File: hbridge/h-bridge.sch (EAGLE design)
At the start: 7 parts

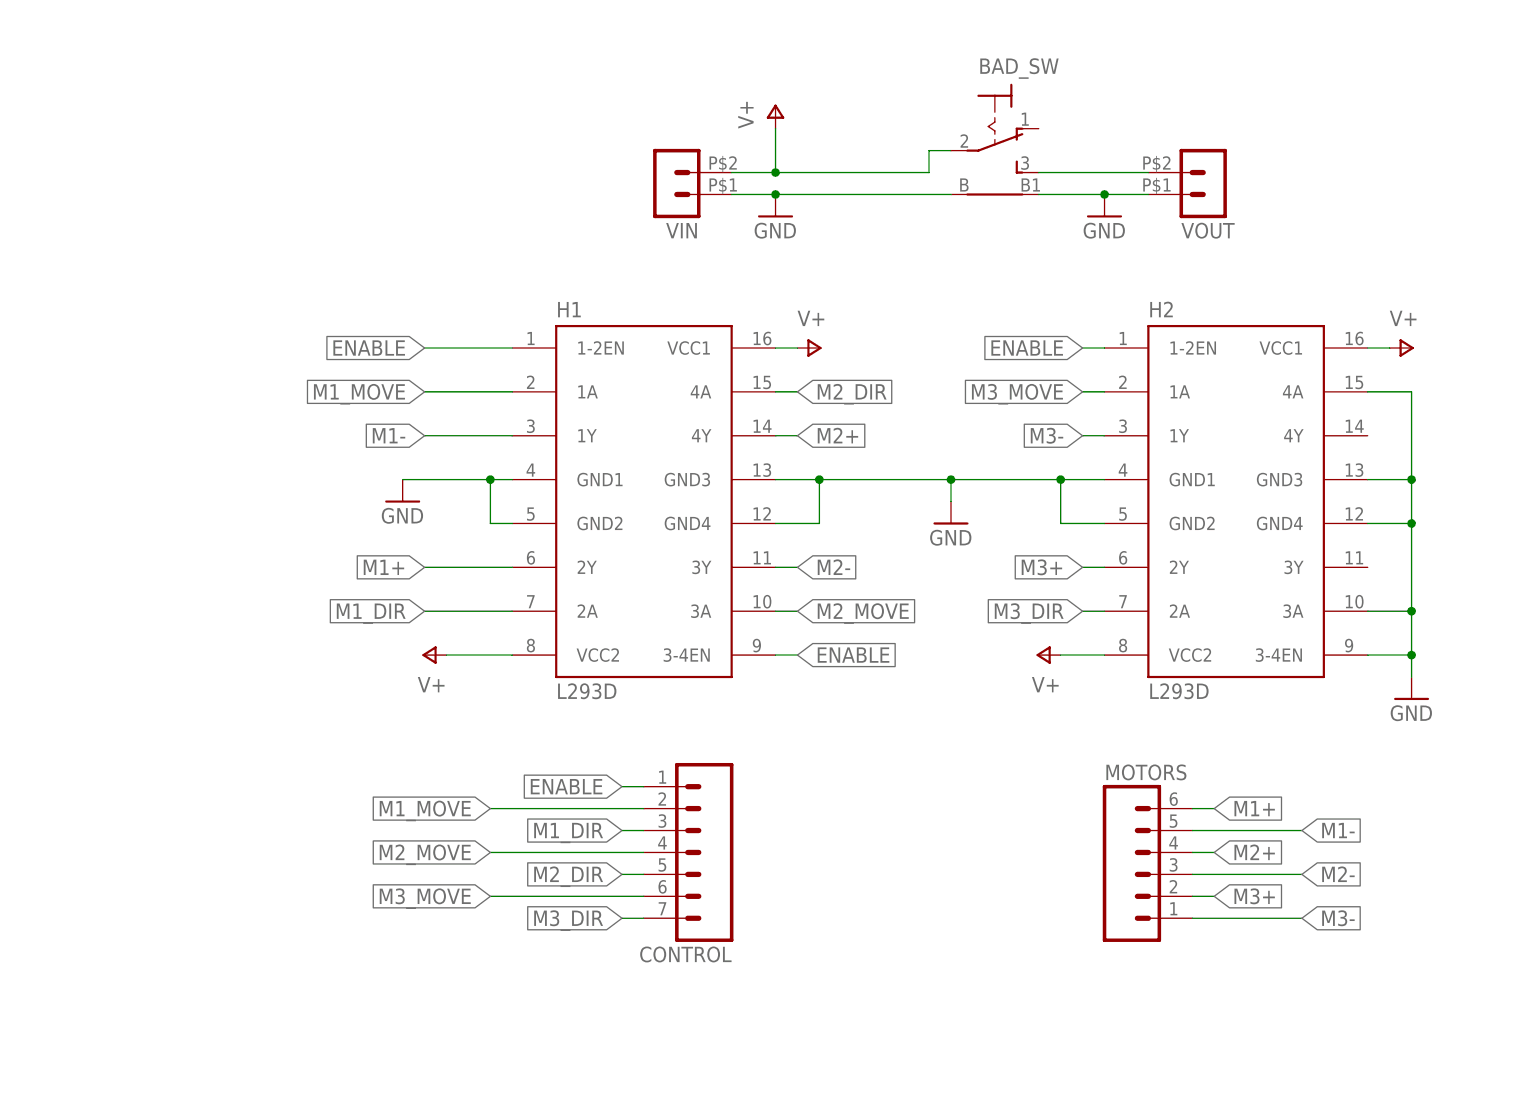
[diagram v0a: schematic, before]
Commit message: Rework H-bridge to add charge port, move headers to back
- correct hole sizes and placement
- added key dimension documentation
- switch toggles battery between circuit and charge port
- headers on backside leading toward center of chassis
- battery in and daisy chain output also point into center
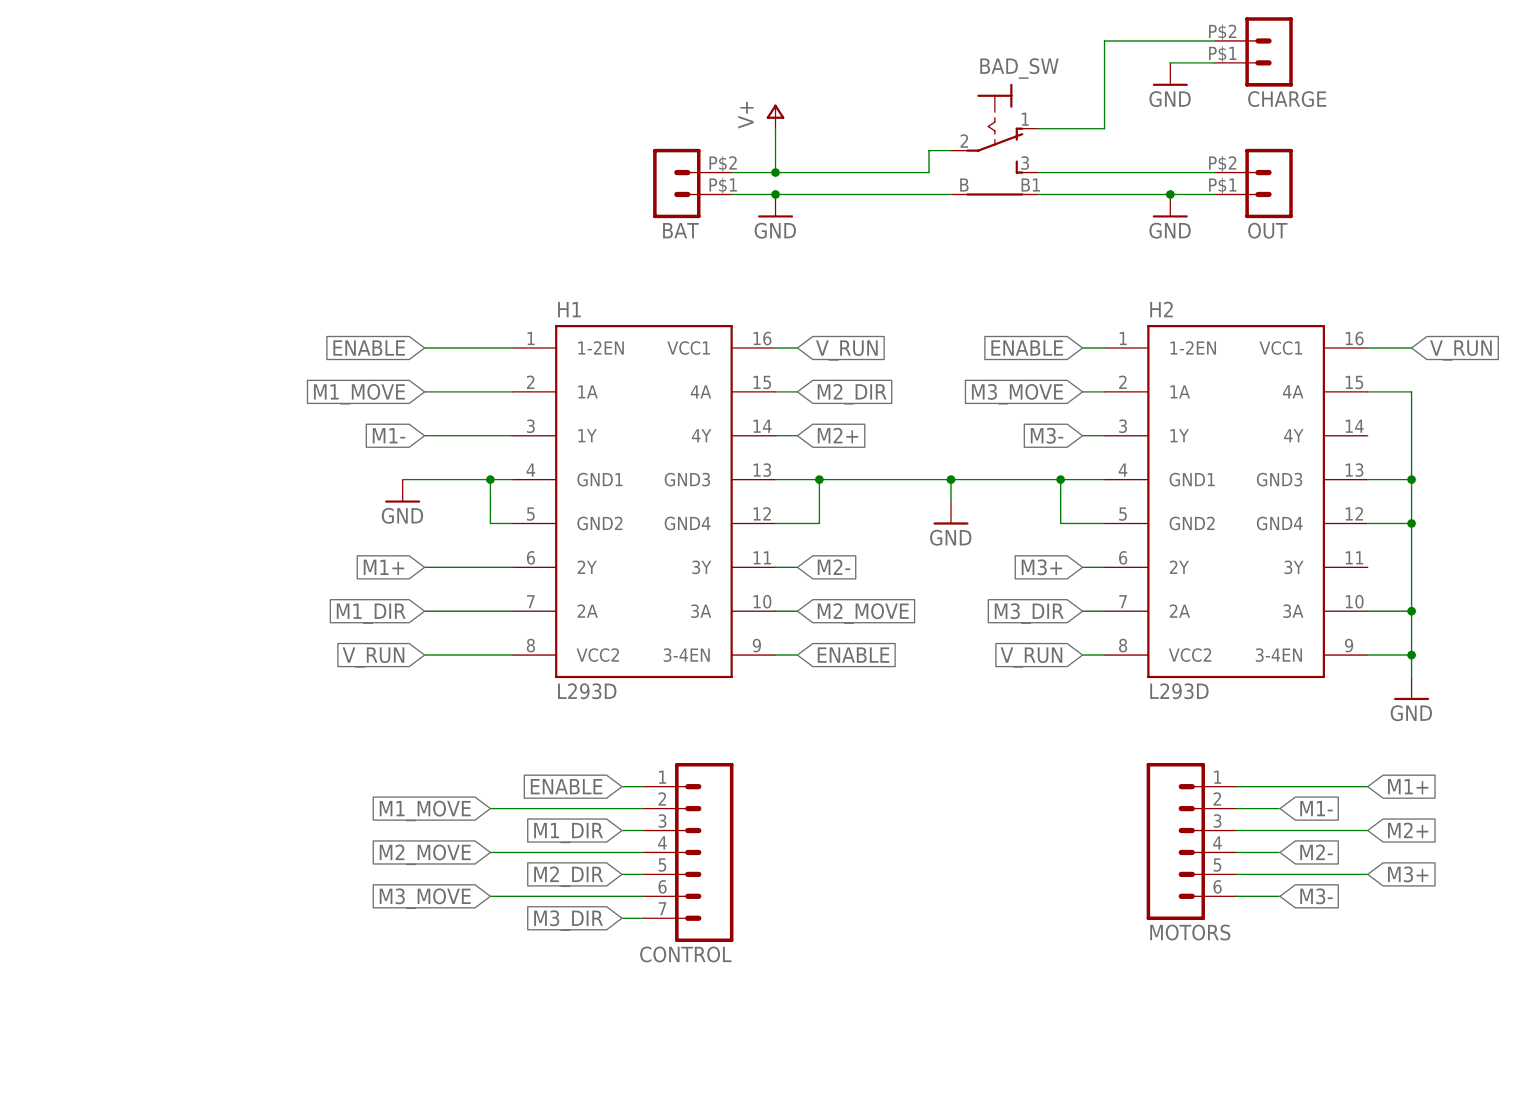
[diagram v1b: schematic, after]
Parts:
- removed VOUT: (no value), con-molex-micro-fit-3_0:HEADER_POS2_43045-0206
- added CHARGE, OUT: (no value), con-molex-micro-fit-3_0:HEADER_POS2_43045-0206
- CONTROL: device SparkFun-Connectors:M07LOCK_LONGPADS -> SparkFun-Connectors:M07LOCK
- MOTORS: device SparkFun-Connectors:M06LOCK_LONGPADS -> SparkFun-Connectors:M06LOCK
- renumbered VIN to BAT
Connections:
- removed net N$3: BAD_SW.S, VOUT.2
- new net V_CHARGE: BAD_SW.O, CHARGE.2
- new net V_RUN: BAD_SW.S, H1.VCC1, OUT.2
- net GND: now also CHARGE.1, OUT.1; no longer VOUT.1
- net M1+: now also MOTORS.1; no longer MOTORS.6
- net M1-: now also MOTORS.2; no longer MOTORS.5
- net M2+: now also MOTORS.3; no longer MOTORS.4
- net M2-: now also MOTORS.4; no longer MOTORS.3
- net M3+: now also MOTORS.5; no longer MOTORS.2
- net M3-: now also MOTORS.6; no longer MOTORS.1
- net V+: no longer H1.VCC1, H1.VCC2, H2.VCC1, H2.VCC2
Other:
- moved on the sheet: MOTORS

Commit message: Fix V_RUN net so that it is actually attached to ICs
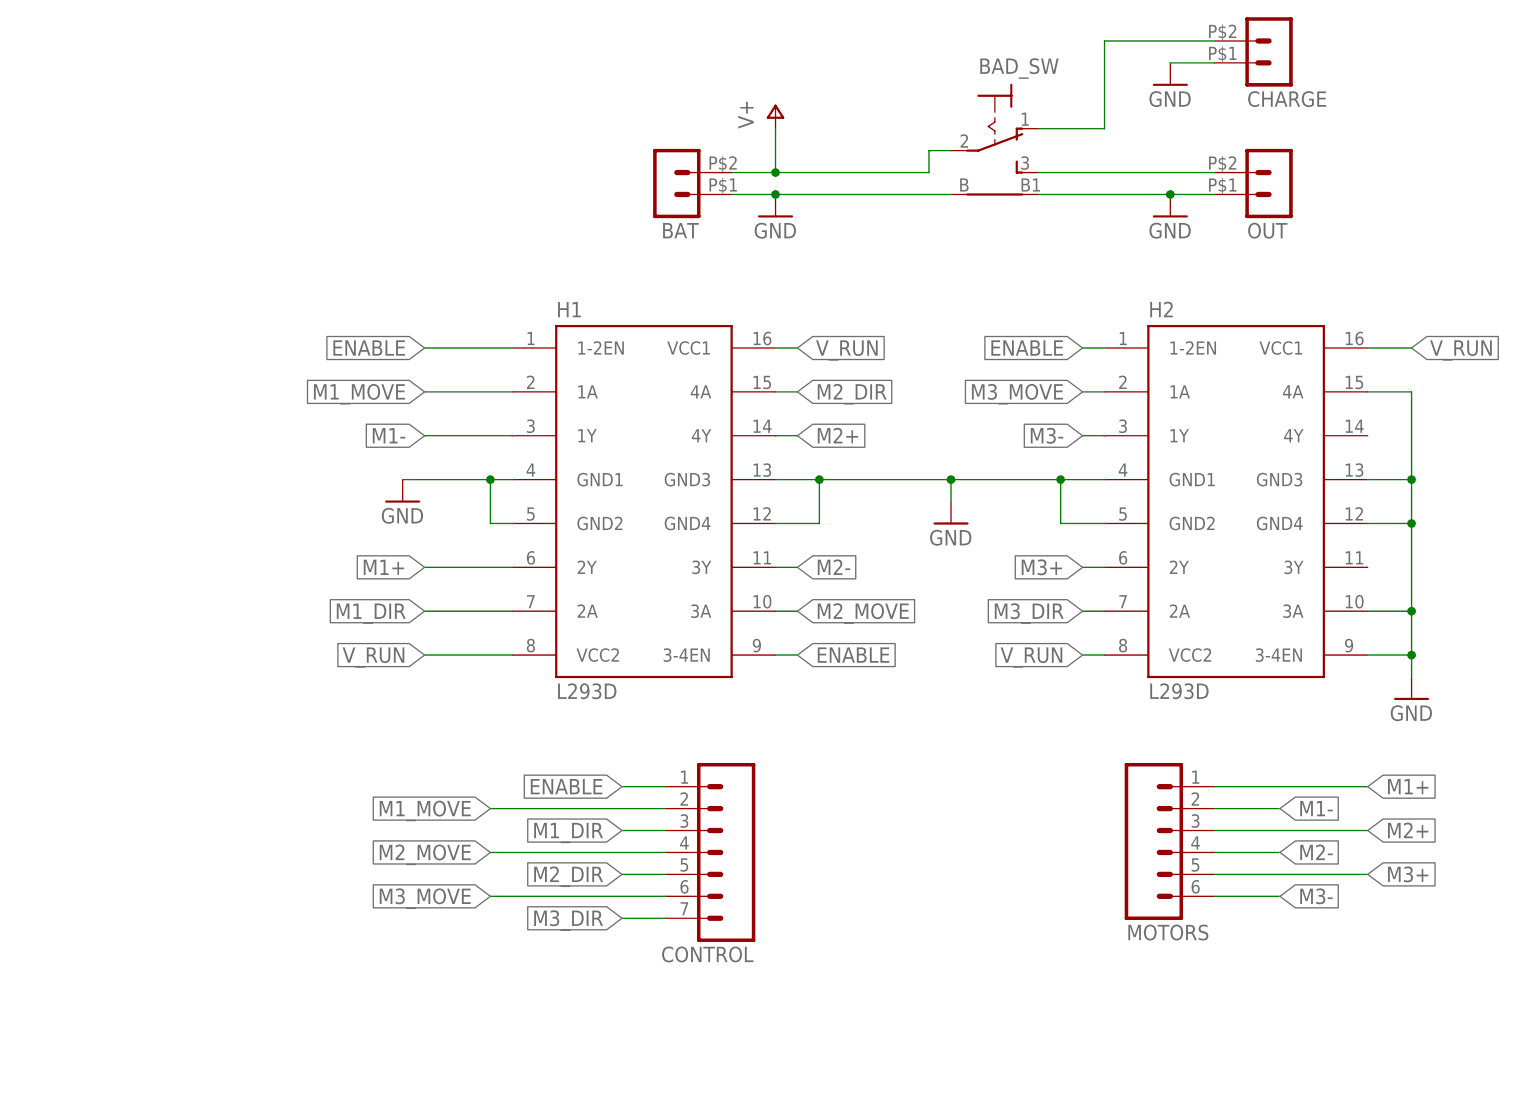
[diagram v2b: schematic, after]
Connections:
- net V_RUN: now also H1.VCC2, H2.VCC1, H2.VCC2
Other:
- moved on the sheet: CONTROL, MOTORS

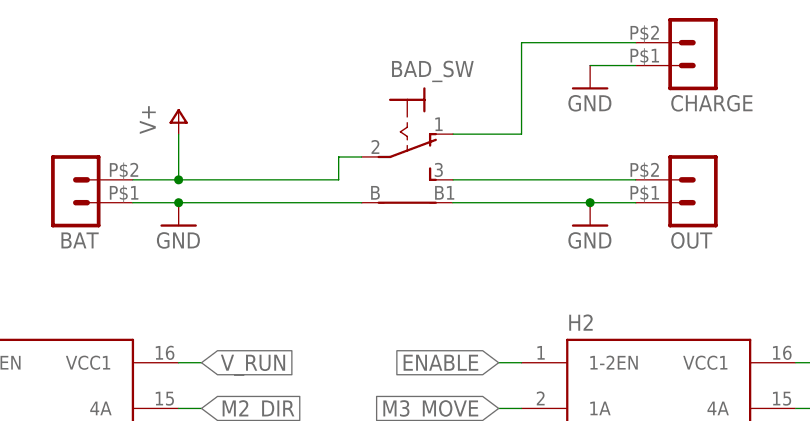
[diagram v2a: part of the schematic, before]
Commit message: Update H-bridge board to use correct switch
- The E-switch WSP1 is a custom model from the wolfbot.lbr library
- Shifted most components due to the larger switch footprint
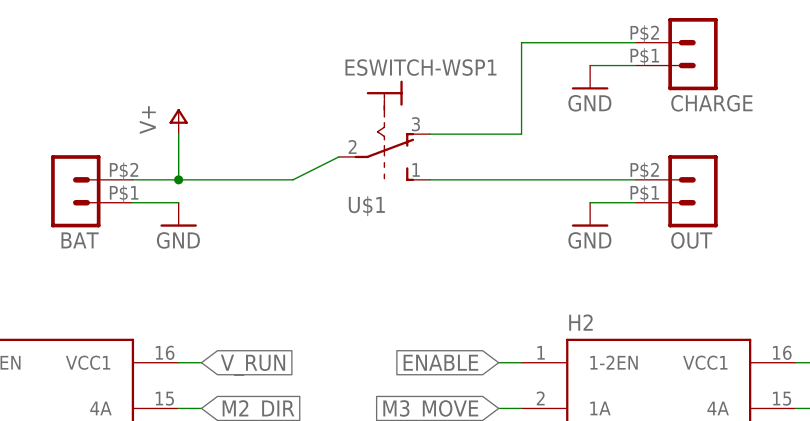
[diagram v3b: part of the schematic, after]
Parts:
- removed BAD_SW: (no value), switch:9070-1W
- added U$1: ESWITCH-WSP1, wolfbot:ESWITCH-WSP1
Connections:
- net GND: no longer BAD_SW.B, BAD_SW.B1
- net V+: now also U$1.2; no longer BAD_SW.P
- net V_CHARGE: now also U$1.3; no longer BAD_SW.O
- net V_RUN: now also U$1.1; no longer BAD_SW.S
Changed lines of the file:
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@@
 <part name="GND4" library="supply1" deviceset="GND" device=""/>
 <part name="GND5" library="supply1" deviceset="GND" device=""/>
-<part name="BAD_SW" library="switch" deviceset="9070-1W" device=""/>
 <part name="GND3" library="supply1" deviceset="GND" device=""/>
 <part name="CHARGE" library="con-molex-micro-fit-3_0" deviceset="HEADER_POS2_?" device="43045-0206"/>
 <part name="GND6" library="supply1" deviceset="GND" device=""/>
+<part name="U$1" library="wolfbot" deviceset="ESWITCH-WSP1" device=""/>
 </parts>
 <sheets>
@@
 <instance part="GND4" gate="1" x="20.32" y="71.12"/>
 <instance part="GND5" gate="1" x="137.16" y="48.26"/>
-<instance part="BAD_SW" gate="2" x="88.9" y="114.3" rot="R270"/>
 <instance part="GND3" gate="1" x="109.22" y="104.14"/>
 <instance part="CHARGE" gate="G$1" x="119.38" y="124.46" rot="MR180"/>
 <instance part="GND6" gate="1" x="109.22" y="119.38"/>
+<instance part="U$1" gate="G$1" x="83.82" y="111.76"/>
 </instances>
 <busses>
@@
 <pinref part="GND2" gate="1" pin="GND"/>
 <wire x1="58.42" y1="106.68" x2="63.5" y2="106.68" width="0.1524" layer="91"/>
-<pinref part="BAD_SW" gate="2" pin="B"/>
-<wire x1="63.5" y1="106.68" x2="83.82" y2="106.68" width="0.1524" layer="91"/>
-<junction x="63.5" y="106.68"/>
-</segment>
-<segment>
-<pinref part="BAD_SW" gate="2" pin="B1"/>
+</segment>
+<segment>
 <pinref part="OUT" gate="G$1" pin="1"/>
-<wire x1="93.98" y1="106.68" x2="109.22" y2="106.68" width="0.1524" layer="91"/>
 <pinref part="GND3" gate="1" pin="GND"/>
 <wire x1="109.22" y1="106.68" x2="114.3" y2="106.68" width="0.1524" layer="91"/>
-<junction x="109.22" y="106.68"/>
 </segment>
 <segment>
@@
 <pinref part="P+1" gate="1" pin="V+"/>
 <wire x1="63.5" y1="114.3" x2="63.5" y2="109.22" width="0.1524" layer="91"/>
-<wire x1="63.5" y1="109.22" x2="81.28" y2="109.22" width="0.1524" layer="91"/>
+<wire x1="63.5" y1="109.22" x2="76.2" y2="109.22" width="0.1524" layer="91"/>
 <junction x="63.5" y="109.22"/>
-<pinref part="BAD_SW" gate="2" pin="P"/>
-<wire x1="83.82" y1="111.76" x2="81.28" y2="111.76" width="0.1524" layer="91"/>
-<wire x1="81.28" y1="111.76" x2="81.28" y2="109.22" width="0.1524" layer="91"/>
+<wire x1="81.28" y1="111.76" x2="76.2" y2="109.22" width="0.1524" layer="91"/>
+<pinref part="U$1" gate="G$1" pin="2"/>
 </segment>
 </net>
@@
 <net name="V_RUN" class="1">
 <segment>
-<pinref part="BAD_SW" gate="2" pin="S"/>
 <pinref part="OUT" gate="G$1" pin="2"/>
-<wire x1="93.98" y1="109.22" x2="114.3" y2="109.22" width="0.1524" layer="91"/>
+<wire x1="91.44" y1="109.22" x2="114.3" y2="109.22" width="0.1524" layer="91"/>
+<pinref part="U$1" gate="G$1" pin="1"/>
 </segment>
 <segment>
@@
 <net name="V_CHARGE" class="1">
 <segment>
-<pinref part="BAD_SW" gate="2" pin="O"/>
-<wire x1="93.98" y1="114.3" x2="101.6" y2="114.3" width="0.1524" layer="91"/>
+<wire x1="91.44" y1="114.3" x2="101.6" y2="114.3" width="0.1524" layer="91"/>
 <wire x1="101.6" y1="114.3" x2="101.6" y2="124.46" width="0.1524" layer="91"/>
 <pinref part="CHARGE" gate="G$1" pin="2"/>
 <wire x1="101.6" y1="124.46" x2="114.3" y2="124.46" width="0.1524" layer="91"/>
-</segment>
-</net>
+<pinref part="U$1" gate="G$1" pin="3"/>
+</segment>
+</net>
